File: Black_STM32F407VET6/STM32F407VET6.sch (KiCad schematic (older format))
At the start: 95 parts, among them J1 T0, J10 - HotBed +, J11 Heater0, J12 X-, J13 Y-, J14 Z-, J15 Z+, J16 USB_B, J17 LeftSpi, J2 T1, J23 EXP2, J24 LCD2004, J25 Bottom, J26 Right, J28 LIGHTS, J29 Z, J3 TB, J30 Z, J38 X, J39 Y, J4 TC, J41 E0, J43 Heater1, J44 COM, J47 I2C, J48 SPI, J49 SPI, J5 + VIN -, J50 SDIO, J51 Servo, J52 Servo, J53 PowerSelect, J54 Power, J55 PD11, J56 Power, J6 Fan3, J7 Fan2, J8 Fan1, J9 Fan0, Q1 BCX70, Q10 BCX70, Q11 BCX70, Q12 IRLR8726PBF, Q13 IRLR8726PBF, Q14 IRLR8726PBF, Q2 BCX70, Q3 BCX70, Q4 IRLML0030TRPBF, Q5 BCX70, Q6 IRLML0030TRPBF, Q7 IRLML0030TRPBF, Q8 IRLML0030TRPBF, Q9 BCX70, SW1 Boot0, U1 LeftAnalog, U2 Left5V, U5 AT24CS01-SSHM

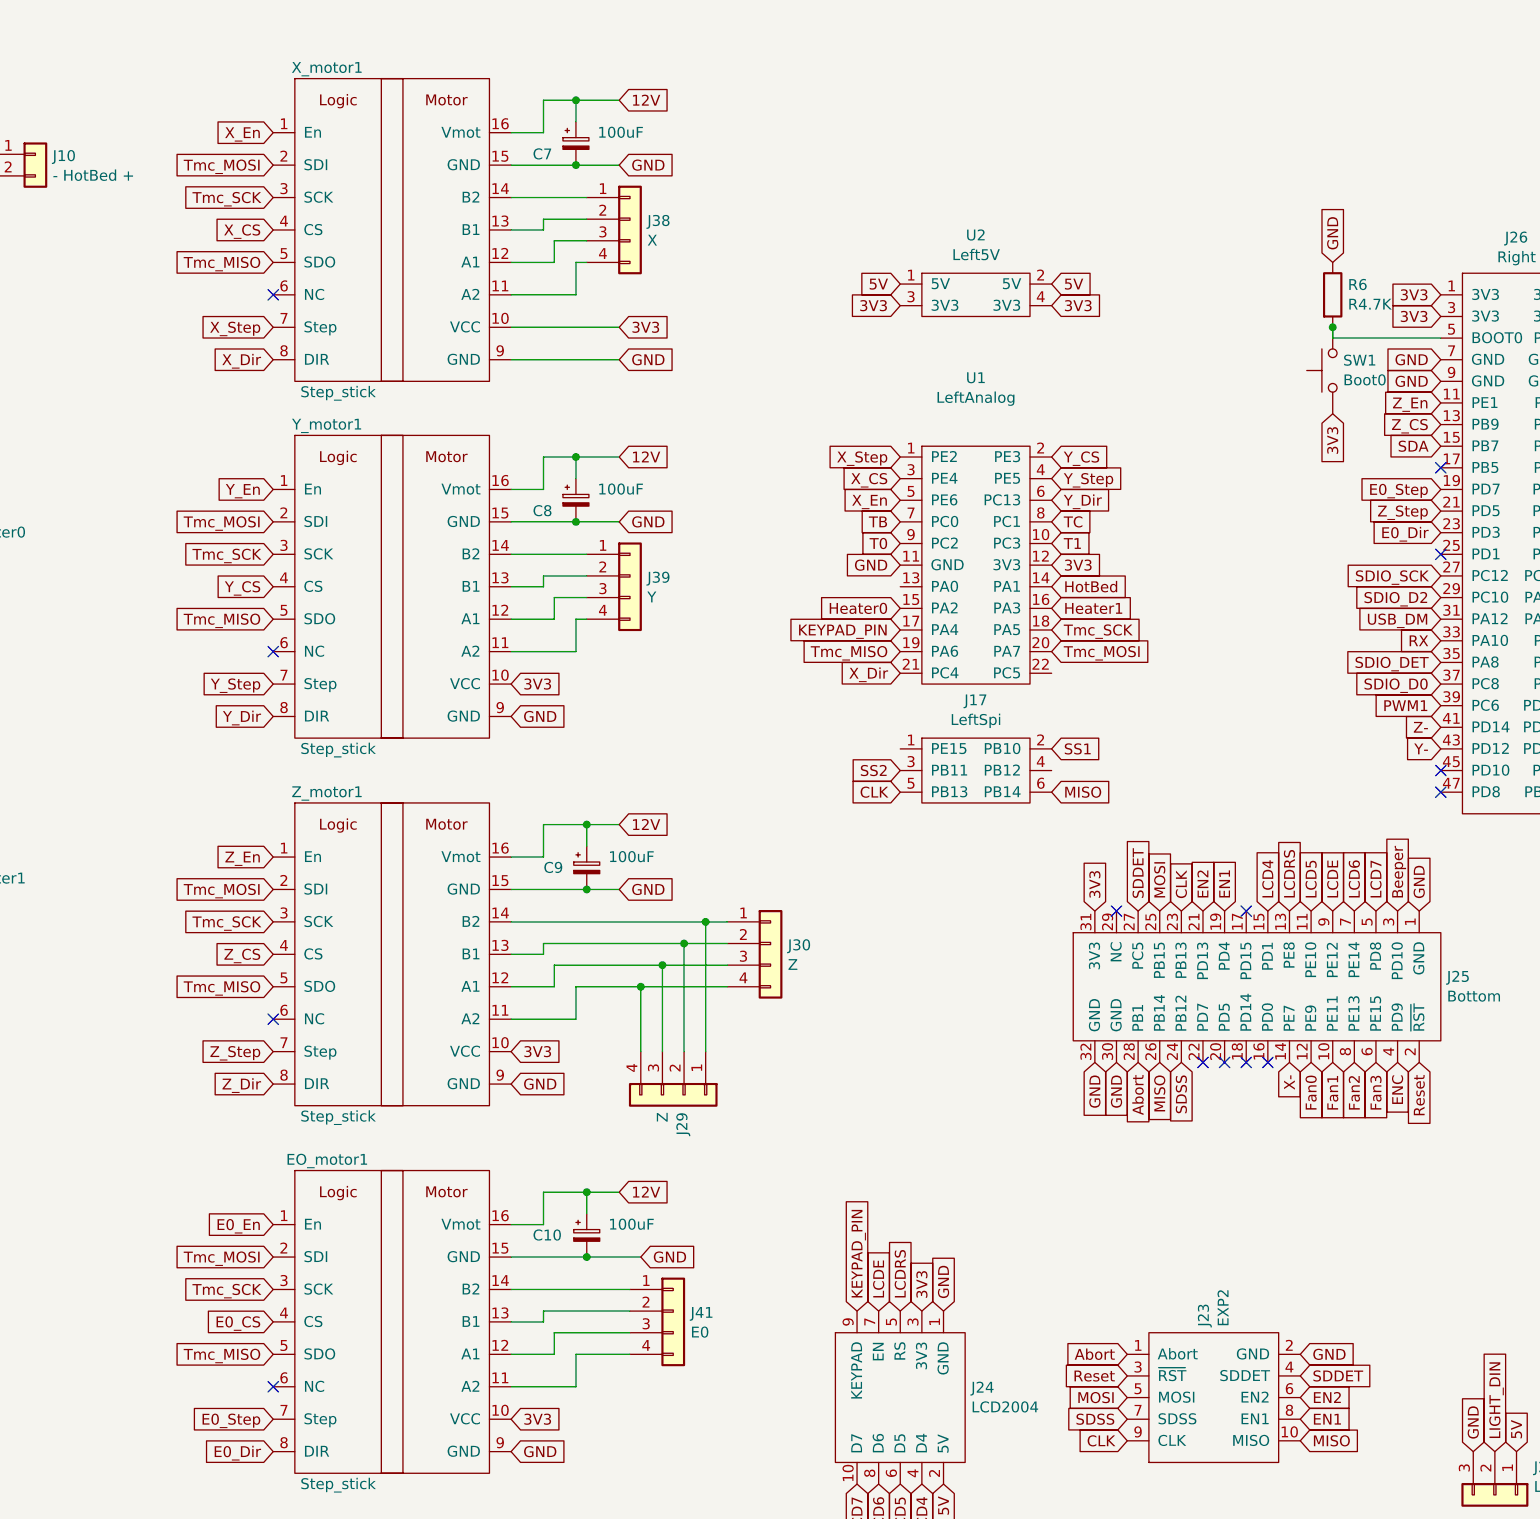
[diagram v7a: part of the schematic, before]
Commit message: Changed spi channel, updated design rules TODO: change all tracks to be at least 0.25 wide and fix tracks not being in the center between headers
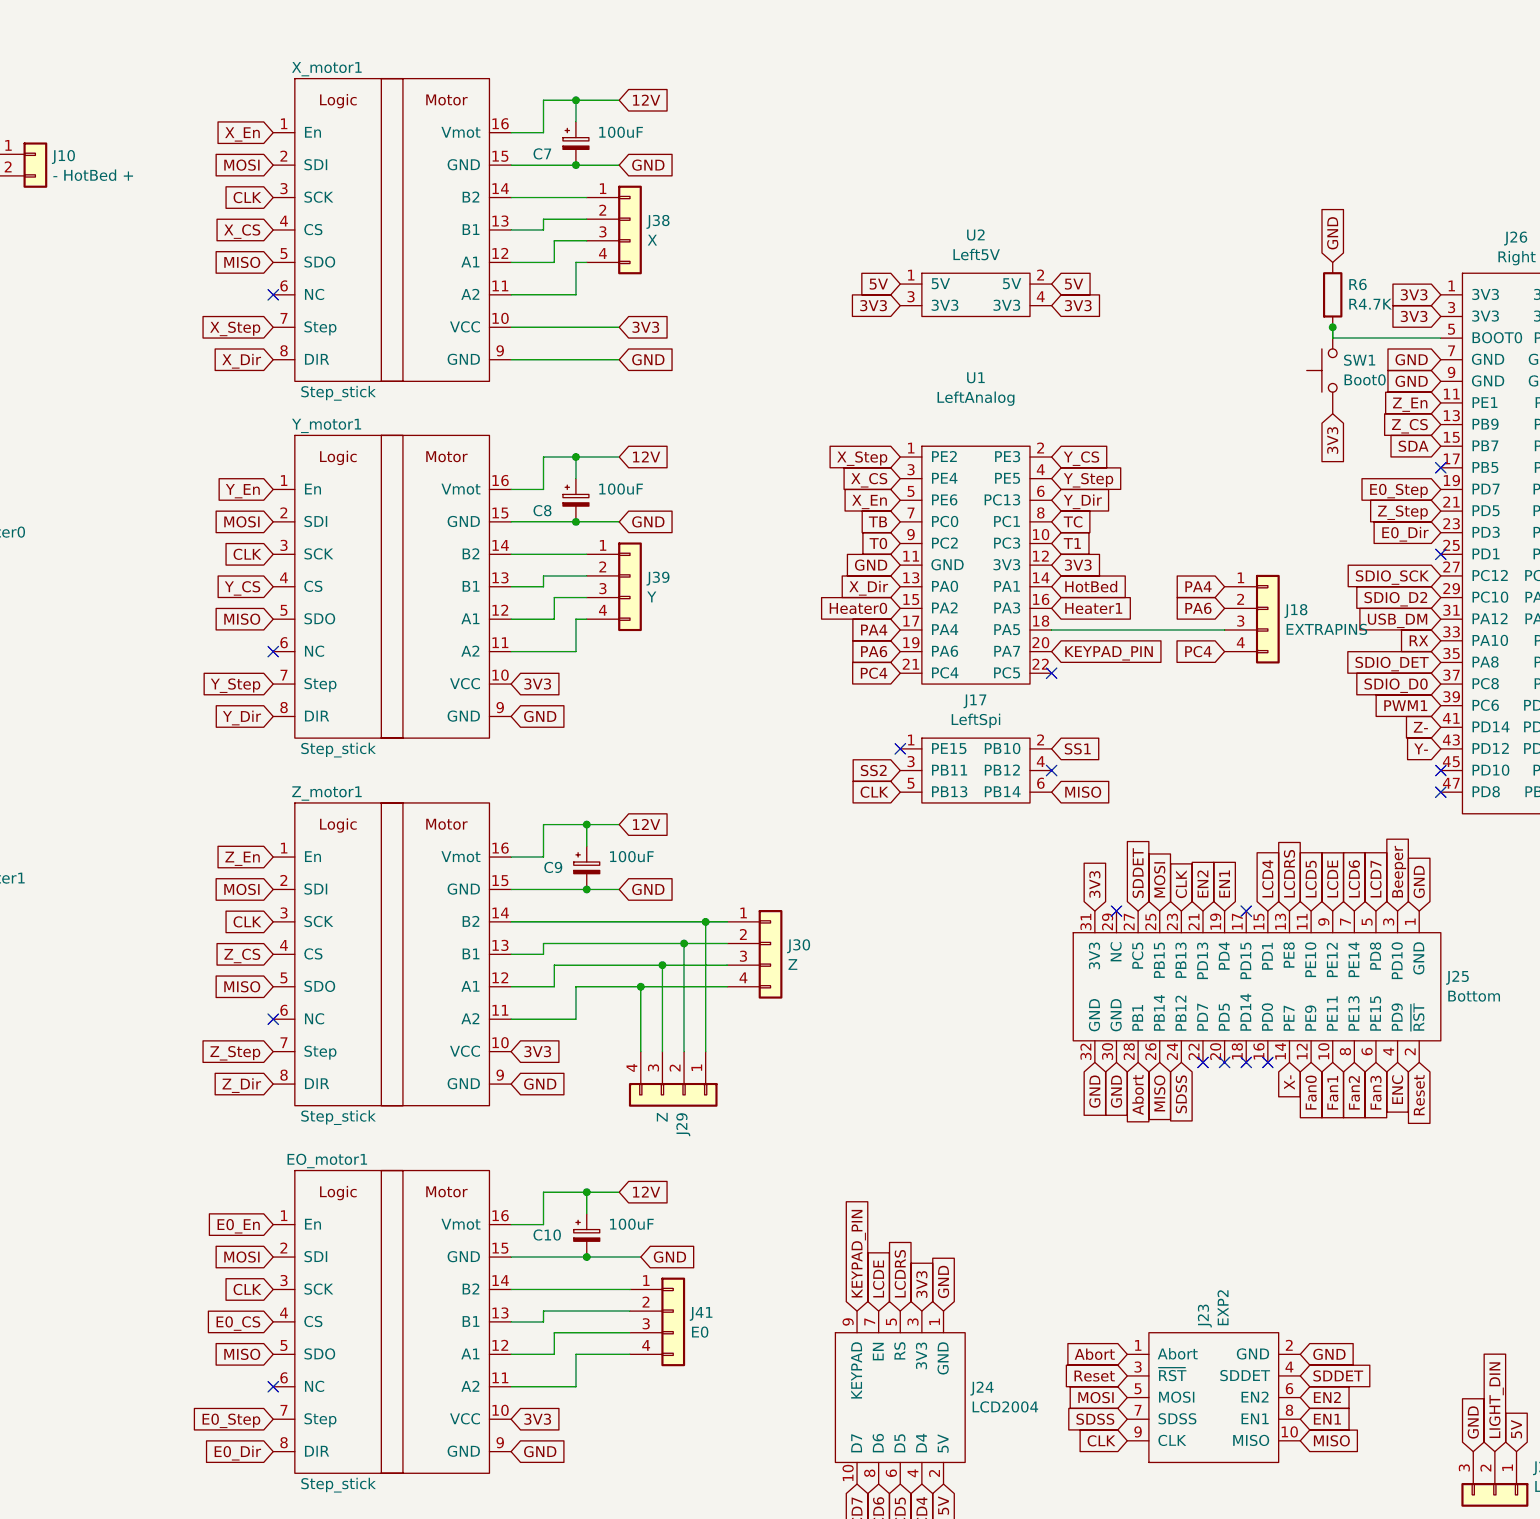
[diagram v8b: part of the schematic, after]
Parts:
- added J18: EXTRAPINS, Connector_PinHeader_2.54mm:PinHeader_1x04_P2.54mm_Vertical, symbol Connector_Generic:Conn_01x04
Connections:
- net CLK: now also EO_motor1.3 (SCK), X_motor1.3 (SCK), Y_motor1.3 (SCK), Z_motor1.3 (SCK)
- net KEYPAD_PIN: now also U1.20 (PA7); no longer U1.17 (PA4)
- net MISO: now also EO_motor1.5 (SDO), X_motor1.5 (SDO), Y_motor1.5 (SDO), Z_motor1.5 (SDO)
- net MOSI: now also EO_motor1.2 (SDI), X_motor1.2 (SDI), Y_motor1.2 (SDI), Z_motor1.2 (SDI)
- net X_Dir: now also U1.13 (PA0); no longer U1.21 (PC4)
- removed net Tmc_MISO: EO_motor1.5 (SDO), U1.19 (PA6), X_motor1.5 (SDO), Y_motor1.5 (SDO), Z_motor1.5 (SDO)
- removed net Tmc_MOSI: EO_motor1.2 (SDI), U1.20 (PA7), X_motor1.2 (SDI), Y_motor1.2 (SDI), Z_motor1.2 (SDI)
- removed net Tmc_SCK: EO_motor1.3 (SCK), U1.18 (PA5), X_motor1.3 (SCK), Y_motor1.3 (SCK), Z_motor1.3 (SCK)
- new net: J18.3 (Pin_3), U1.18 (PA5)
- new net PA4: J18.1 (Pin_1), U1.17 (PA4)
- new net PA6: J18.2 (Pin_2), U1.19 (PA6)
- new net PC4: J18.4 (Pin_4), U1.21 (PC4)
- no-connect marks 19 -> 22
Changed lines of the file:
@@
 Text GLabel 12000 5600 3    50   Input ~ 0
 Fan3
-Text GLabel 11000 5600 3    50   Input ~ 0
-MISO
 Text GLabel 11100 5600 3    50   Input ~ 0
 SDSS
-Text GLabel 11100 4900 1    50   Input ~ 0
-CLK
 Text GLabel 10900 4900 1    50   Input ~ 0
 SDDET
@@
 Text GLabel 6900 7400 0    50   Input ~ 0
 E0_Dir
-Text GLabel 11000 4900 1    50   Input ~ 0
-MOSI
 NoConn ~ 11200 5600
 NoConn ~ 11300 5600
@@
 	0    1    1    0
 $EndComp
-Text GLabel 6900 1900 0    50   Input ~ 0
-Tmc_MISO
-Text GLabel 6900 3550 0    50   Input ~ 0
-Tmc_MISO
-Text GLabel 6900 5250 0    50   Input ~ 0
-Tmc_MISO
-Text GLabel 6900 6950 0    50   Input ~ 0
-Tmc_MISO
-Text GLabel 6900 1450 0    50   Input ~ 0
-Tmc_MOSI
-Text GLabel 6900 3100 0    50   Input ~ 0
-Tmc_MOSI
-Text GLabel 6900 4800 0    50   Input ~ 0
-Tmc_MOSI
-Text GLabel 6900 6500 0    50   Input ~ 0
-Tmc_MOSI
-Text GLabel 6900 1600 0    50   Input ~ 0
-Tmc_SCK
-Text GLabel 6900 3250 0    50   Input ~ 0
-Tmc_SCK
-Text GLabel 6900 4950 0    50   Input ~ 0
-Tmc_SCK
-Text GLabel 6900 6650 0    50   Input ~ 0
-Tmc_SCK
 Text GLabel 6900 1750 0    50   Input ~ 0
 X_CS
@@
 Text GLabel 10500 4150 2    50   Input ~ 0
 SS1
-Text GLabel 10500 4350 2    50   Input ~ 0
-MISO
-Text GLabel 9800 4350 0    50   Input ~ 0
-CLK
 Text GLabel 9800 4250 0    50   Input ~ 0
 SS2
@@
 Text GLabel 10500 3500 2    50   Input ~ 0
 Heater1
-Text GLabel 10500 3600 2    50   Input ~ 0
-Tmc_SCK
-Text GLabel 10500 3700 2    50   Input ~ 0
-Tmc_MOSI
 Text GLabel 10500 2800 2    50   Input ~ 0
 Y_CS
@@
 Text GLabel 9800 3500 0    50   Input ~ 0
 Heater0
-Text GLabel 9800 3800 0    50   Input ~ 0
-X_Dir
 Text GLabel 9800 2800 0    50   Input ~ 0
 X_Step
 Text GLabel 9800 3000 0    50   Input ~ 0
 X_En
-Text GLabel 9800 3700 0    50   Input ~ 0
-Tmc_MISO
 Text GLabel 9800 2900 0    50   Input ~ 0
 X_CS
-Text GLabel 9800 3600 0    50   Input ~ 0
+Text GLabel 10500 3700 2    50   Input ~ 0
 KEYPAD_PIN
 $Comp
@@
 	1    0    0    -1
 $EndComp
+Text GLabel 9800 4350 0    50   Input ~ 0
+CLK
+Text GLabel 10500 4350 2    50   Input ~ 0
+MISO
+Text GLabel 11000 4900 1    50   Input ~ 0
+MOSI
+Text GLabel 11100 4900 1    50   Input ~ 0
+CLK
+Text GLabel 11000 5600 3    50   Input ~ 0
+MISO
+Text GLabel 6900 6500 0    50   Input ~ 0
+MOSI
+Text GLabel 6900 6950 0    50   Input ~ 0
+MISO
+Text GLabel 6900 6650 0    50   Input ~ 0
+CLK
+Text GLabel 6900 1900 0    50   Input ~ 0
+MISO
+Text GLabel 6900 1600 0    50   Input ~ 0
+CLK
+Text GLabel 6900 1450 0    50   Input ~ 0
+MOSI
+Text GLabel 6900 5250 0    50   Input ~ 0
+MISO
+Text GLabel 6900 4950 0    50   Input ~ 0
+CLK
+Text GLabel 6900 4800 0    50   Input ~ 0
+MOSI
+Text GLabel 6900 3550 0    50   Input ~ 0
+MISO
+Text GLabel 6900 3250 0    50   Input ~ 0
+CLK
+Text GLabel 6900 3100 0    50   Input ~ 0
+MOSI
+NoConn ~ 10500 4250
+NoConn ~ 9800 4150
+NoConn ~ 10500 3800
+$Comp
+L Connector_Generic:Conn_01x04 J18
+U 1 1 5D4B6054
+P 11500 3500
+F 0 "J18" H 11580 3492 50  0000 L CNN
+F 1 "EXTRAPINS" H 11580 3401 50  0000 L CNN
+F 2 "Connector_PinHeader_2.54mm:PinHeader_1x04_P2.54mm_Vertical" H 11500 3500 50  0001 C CNN
+F 3 "~" H 11500 3500 50  0001 C CNN
+	1    11500 3500
+	1    0    0    -1
+$EndComp
+Wire Wire Line
+	10500 3600 11300 3600
+Text GLabel 9800 3600 0    50   Input ~ 0
+PA4
+Text GLabel 11300 3400 0    50   Input ~ 0
+PA4
+Text GLabel 9800 3700 0    50   Input ~ 0
+PA6
+Text GLabel 11300 3500 0    50   Input ~ 0
+PA6
+Text GLabel 9800 3400 0    50   Input ~ 0
+X_Dir
+Text GLabel 11300 3700 0    50   Input ~ 0
+PC4
+Text GLabel 9800 3800 0    50   Input ~ 0
+PC4
 $EndSCHEMATC
